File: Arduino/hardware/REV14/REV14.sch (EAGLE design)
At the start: 23 parts, among them IC2 ATMEGA168-AU, Q1 32768Hz, U2 RFM95WSMD

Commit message: updated rev 14
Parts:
- removed ANT: ANT (86 mm), wirepad:2,15/1,0
- removed C11: 100nF, resistor:C-EUC0603
- removed C8: 100u, SparkFun-Passives:CAP_POL1206
- removed R12, R5: 4.7K, resistor:R-EU_R0603
- removed U2: RFM95WSMD, misiek:RFM95WSMD
- added C5: 100nF, resistor:C-EUC0603
- added DQ: (no value), wirepad:2,15/1,0
- added R3: 4.7K, resistor:R-EU_R0603
- added U1: RN2483, RFM95W-RN2483:RN2483
- I2C_EXT: device pinhead:PINHD-2X7 -> pinhead:PINHD-2X10
- renumbered PHT1 to PHT, U$4 to U4
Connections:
- removed net N$22: ANT.P, U2.ANT
- new net RN2483_RESET: IC2.DIGITAL_5(PWM)
- new net RN2483_UART_RX: IC2.DIGITAL_4
- new net RN2483_UART_TX: IC2.DIGITAL_3(PWM)
- net D2: now also DQ.P, I2C_EXT.17; no longer I2C_EXT.14
- net GND: now also I2C_EXT.10, I2C_EXT.12; no longer C8.-, U2.GND@1, U2.GND@2, U2.GND@3
- net IO_POWER_UP: now also I2C_EXT.19
- net N$1: now also I2C_EXT.18, R3.2; no longer C11.2, I2C_EXT.5
- net N$3: now also I2C_EXT.16, R4.2; no longer I2C_EXT.12, R5.2
- net N$4: now also C5.2, I2C_EXT.20; no longer I2C_EXT.11, R4.2
- net RESET: now also C5.1, I2C_EXT.5; no longer C11.1
- net RFM_IRQ: now also I2C_EXT.13; no longer I2C_EXT.7
- net RX: now also R3.1; no longer R4.1
- net SDA: now also I2C_EXT.11; no longer I2C_EXT.10
- net SPI_MISO: no longer U2.MISO
- net SPI_MOSI: no longer U2.MOSI
- net SPI_NSS: now also I2C_EXT.15; no longer I2C_EXT.8, R12.1, U2.NSS
- net SPI_SCK: no longer U2.SCK
- net TX: now also R4.1; no longer R5.1
- net VCC: no longer C8.+, R12.2, U2.VCC
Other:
- note added: "On BOM"
- moved on the sheet: C4, R4

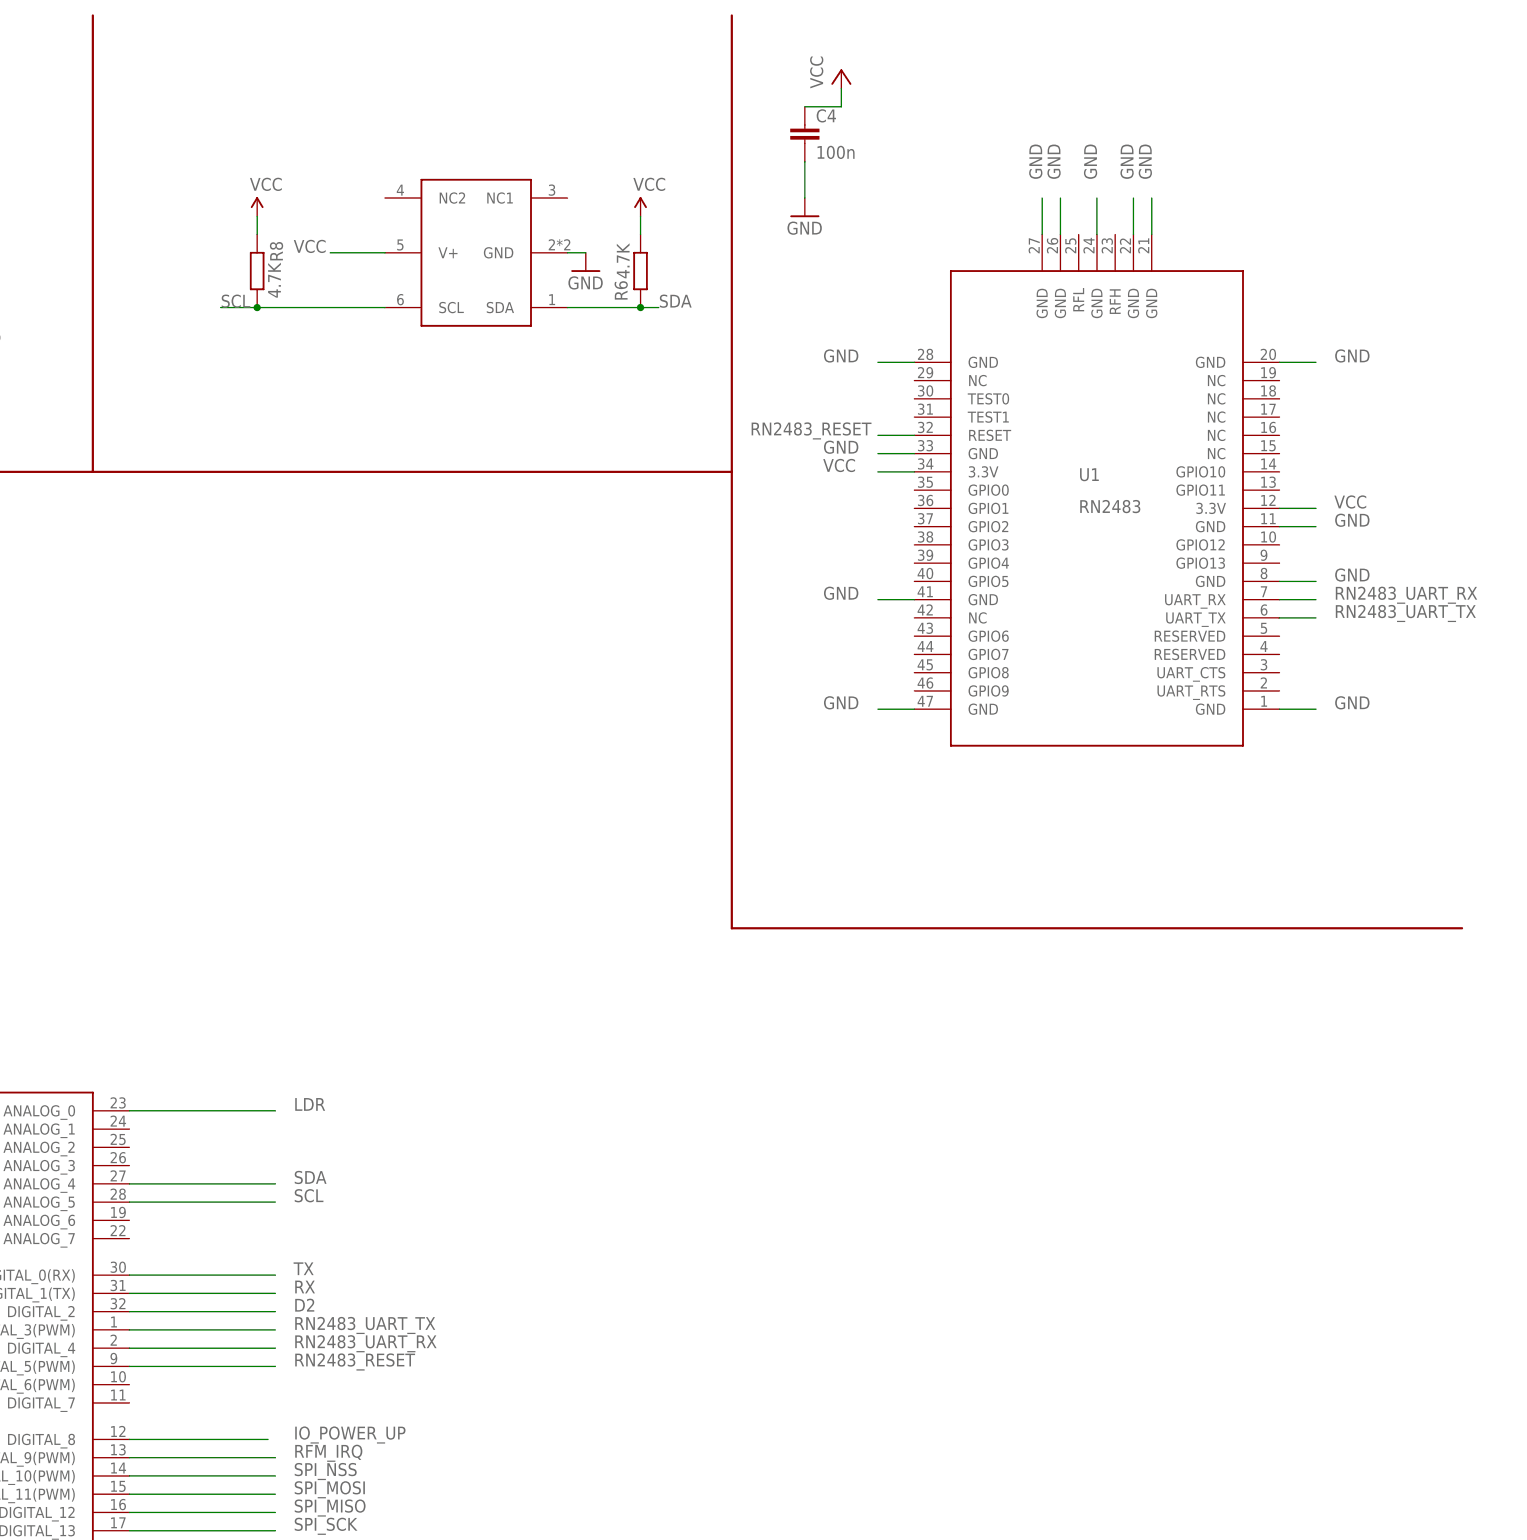
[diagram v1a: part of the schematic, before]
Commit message: rev 14 ant tracks and xtal done
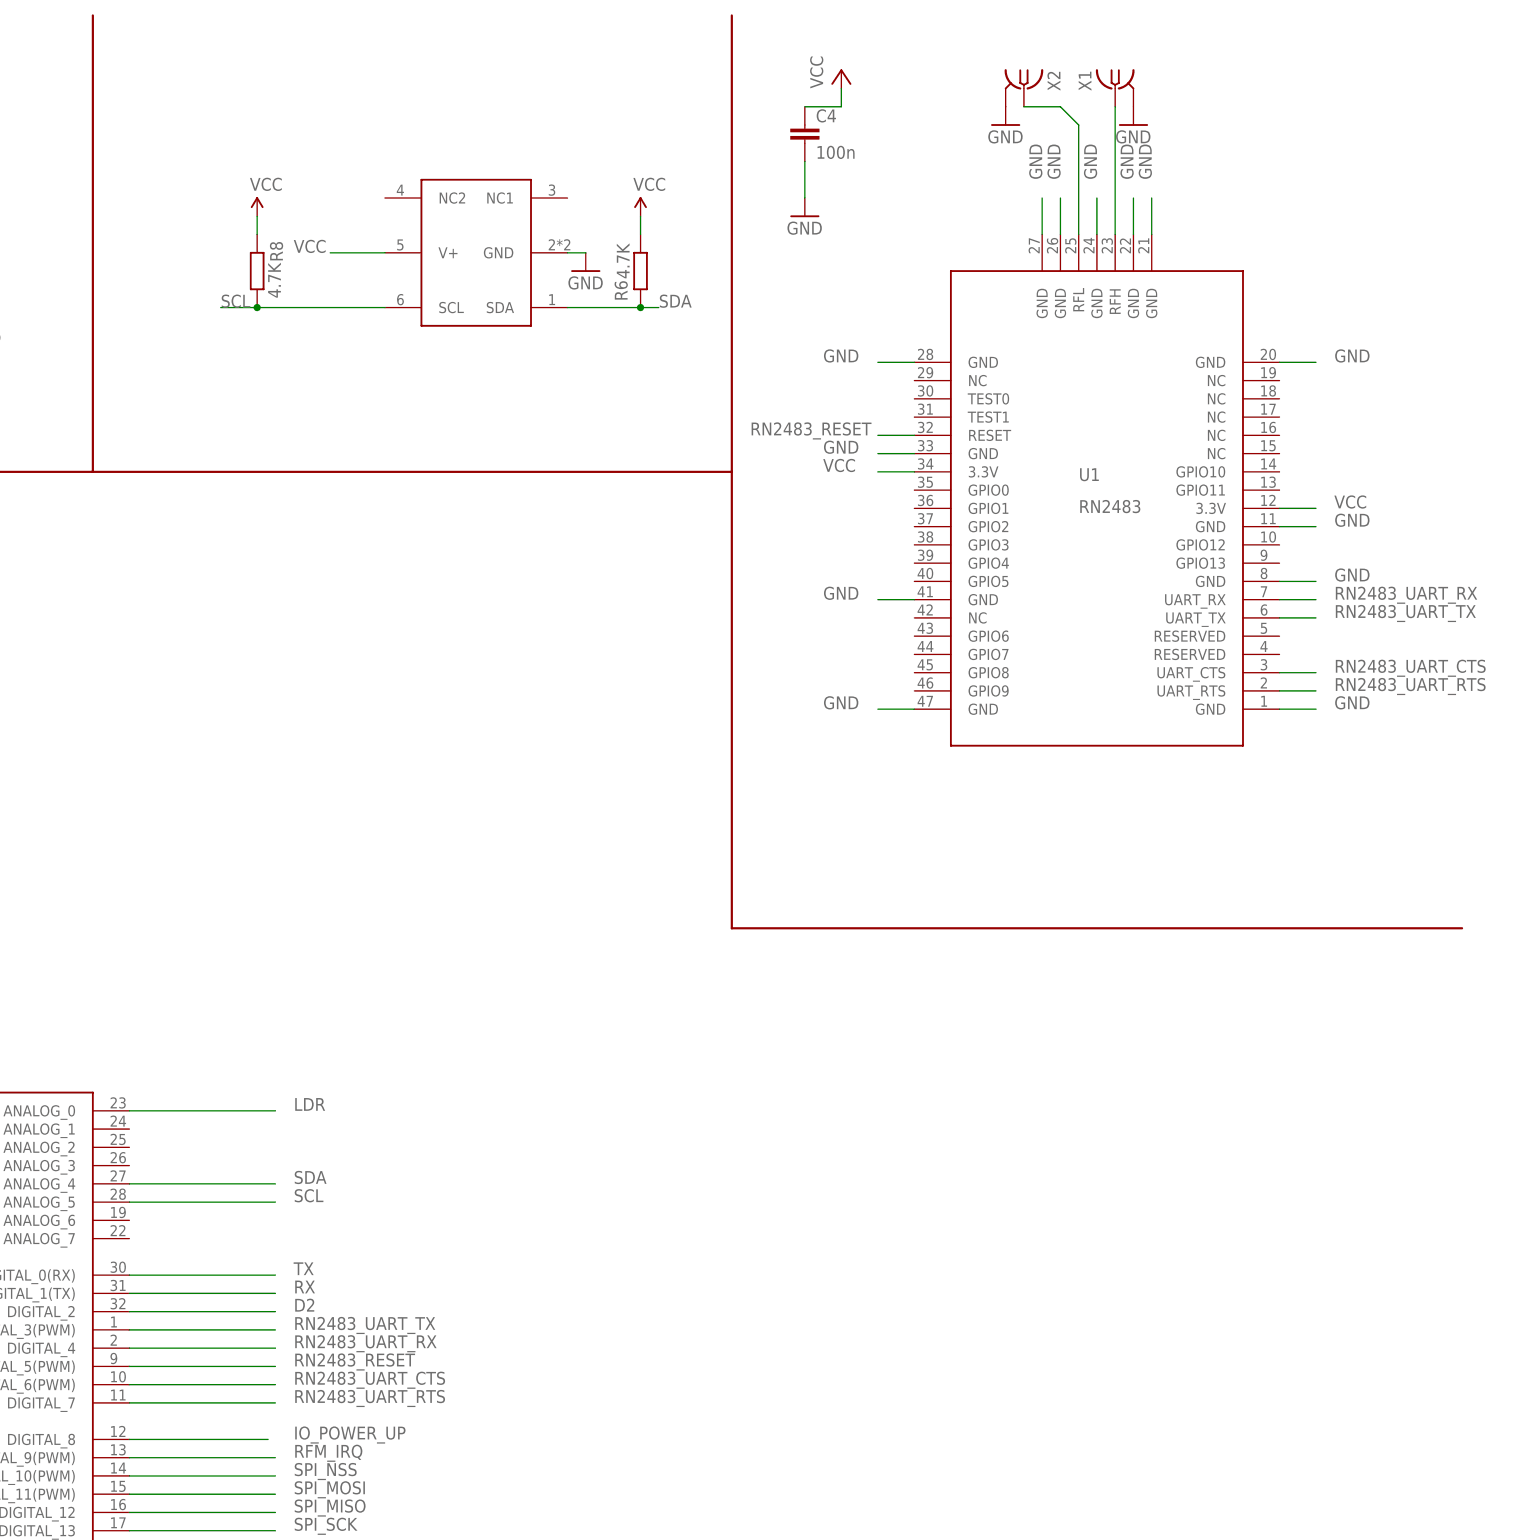
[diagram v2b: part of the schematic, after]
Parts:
- added X1, X2: SMA-142-0701-881/886, con-coax:SMA-142-0701-881/886
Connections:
- new net N$22: U1.RFH, X1.1
- new net N$33: U1.RFL, X2.1
- new net RN2483_UART_CTS: IC2.DIGITAL_6(PWM), U1.UART_CTS
- new net RN2483_UART_RTS: U1.UART_RTS
- net GND: now also U1.GND@1, U1.GND@10, U1.GND@11, U1.GND@12, U1.GND@13, U1.GND@2, U1.GND@3, U1.GND@4, U1.GND@5, U1.GND@6, U1.GND@7, U1.GND@8, U1.GND@9, X1.2, X2.2
- net RN2483_RESET: now also U1.RESET
- net RN2483_UART_RX: now also U1.UART_RX
- net RN2483_UART_TX: now also U1.UART_TX
- net VCC: now also U1.3.3V, U1.3.3V@1
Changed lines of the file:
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@@
 <part name="R4" library="resistor" deviceset="R-EU_" device="R0603" value="4.7K"/>
 <part name="C5" library="resistor" deviceset="C-EU" device="C0603" value="100nF"/>
+<part name="X1" library="con-coax" deviceset="SMA-" device="142-0701-881/886"/>
+<part name="X2" library="con-coax" deviceset="SMA-" device="142-0701-881/886"/>
+<part name="GND4" library="supply1" deviceset="GND" device=""/>
+<part name="GND5" library="supply1" deviceset="GND" device=""/>
 </parts>
 <sheets>
@@
 <attribute name="NAME" x="131.699" y="230.124" size="1.778" layer="95" rot="R90"/>
 </instance>
+<instance part="X1" gate="G1" x="335.28" y="246.38" smashed="yes" rot="MR270">
+<attribute name="NAME" x="331.978" y="248.92" size="1.778" layer="95" rot="MR270"/>
+</instance>
+<instance part="X2" gate="G1" x="322.58" y="246.38" smashed="yes" rot="R270">
+<attribute name="NAME" x="325.882" y="248.92" size="1.778" layer="95" rot="R270"/>
+</instance>
+<instance part="GND4" gate="1" x="320.04" y="241.3"/>
+<instance part="GND5" gate="1" x="337.82" y="241.3"/>
 </instances>
 <busses>
@@
 <wire x1="307.34" y1="208.28" x2="302.26" y2="208.28" width="0.1524" layer="91"/>
 <label x="294.64" y="208.28" size="1.778" layer="95"/>
+<pinref part="U1" gate="G$1" pin="GND@10"/>
 </segment>
 <segment>
 <wire x1="307.34" y1="195.58" x2="302.26" y2="195.58" width="0.1524" layer="91"/>
 <label x="294.64" y="195.58" size="1.778" layer="95"/>
+<pinref part="U1" gate="G$1" pin="GND@11"/>
 </segment>
 <segment>
 <wire x1="307.34" y1="175.26" x2="302.26" y2="175.26" width="0.1524" layer="91"/>
 <label x="294.64" y="175.26" size="1.778" layer="95"/>
+<pinref part="U1" gate="G$1" pin="GND@12"/>
 </segment>
 <segment>
 <wire x1="307.34" y1="160.02" x2="302.26" y2="160.02" width="0.1524" layer="91"/>
 <label x="294.64" y="160.02" size="1.778" layer="95"/>
+<pinref part="U1" gate="G$1" pin="GND@13"/>
 </segment>
 <segment>
 <wire x1="363.22" y1="208.28" x2="358.14" y2="208.28" width="0.1524" layer="91"/>
 <label x="365.76" y="208.28" size="1.778" layer="95"/>
+<pinref part="U1" gate="G$1" pin="GND@4"/>
 </segment>
 <segment>
 <wire x1="363.22" y1="185.42" x2="358.14" y2="185.42" width="0.1524" layer="91"/>
 <label x="365.76" y="185.42" size="1.778" layer="95"/>
+<pinref part="U1" gate="G$1" pin="GND@3"/>
 </segment>
 <segment>
 <wire x1="363.22" y1="177.8" x2="358.14" y2="177.8" width="0.1524" layer="91"/>
 <label x="365.76" y="177.8" size="1.778" layer="95"/>
+<pinref part="U1" gate="G$1" pin="GND@2"/>
 </segment>
 <segment>
 <wire x1="363.22" y1="160.02" x2="358.14" y2="160.02" width="0.1524" layer="91"/>
 <label x="365.76" y="160.02" size="1.778" layer="95"/>
+<pinref part="U1" gate="G$1" pin="GND@1"/>
 </segment>
 <segment>
 <wire x1="340.36" y1="226.06" x2="340.36" y2="231.14" width="0.1524" layer="91"/>
 <label x="340.36" y="233.68" size="1.778" layer="95" rot="R90"/>
+<pinref part="U1" gate="G$1" pin="GND@5"/>
 </segment>
 <segment>
 <wire x1="337.82" y1="226.06" x2="337.82" y2="231.14" width="0.1524" layer="91"/>
 <label x="337.82" y="233.68" size="1.778" layer="95" rot="R90"/>
+<pinref part="U1" gate="G$1" pin="GND@6"/>
 </segment>
 <segment>
 <wire x1="332.74" y1="226.06" x2="332.74" y2="231.14" width="0.1524" layer="91"/>
 <label x="332.74" y="233.68" size="1.778" layer="95" rot="R90"/>
+<pinref part="U1" gate="G$1" pin="GND@7"/>
 </segment>
 <segment>
 <wire x1="327.66" y1="226.06" x2="327.66" y2="231.14" width="0.1524" layer="91"/>
 <label x="327.66" y="233.68" size="1.778" layer="95" rot="R90"/>
+<pinref part="U1" gate="G$1" pin="GND@8"/>
 </segment>
 <segment>
 <wire x1="325.12" y1="226.06" x2="325.12" y2="231.14" width="0.1524" layer="91"/>
 <label x="325.12" y="233.68" size="1.778" layer="95" rot="R90"/>
+<pinref part="U1" gate="G$1" pin="GND@9"/>
 </segment>
 <segment>
@@
 <pinref part="I2C_EXT" gate="A" pin="12"/>
 <label x="114.3" y="223.52" size="1.778" layer="95"/>
+</segment>
+<segment>
+<pinref part="X2" gate="G1" pin="2"/>
+<pinref part="GND4" gate="1" pin="GND"/>
+</segment>
+<segment>
+<pinref part="X1" gate="G1" pin="2"/>
+<pinref part="GND5" gate="1" pin="GND"/>
 </segment>
 </net>
@@
 <wire x1="358.14" y1="187.96" x2="363.22" y2="187.96" width="0.1524" layer="91"/>
 <label x="365.76" y="187.96" size="1.778" layer="95"/>
+<pinref part="U1" gate="G$1" pin="3.3V"/>
 </segment>
 <segment>
 <wire x1="302.26" y1="193.04" x2="307.34" y2="193.04" width="0.1524" layer="91"/>
 <label x="294.64" y="193.04" size="1.778" layer="95"/>
+<pinref part="U1" gate="G$1" pin="3.3V@1"/>
 </segment>
 <segment>
@@
 <wire x1="358.14" y1="172.72" x2="363.22" y2="172.72" width="0.1524" layer="91"/>
 <label x="365.76" y="172.72" size="1.778" layer="95"/>
+<pinref part="U1" gate="G$1" pin="UART_TX"/>
 </segment>
 </net>
@@
 <wire x1="358.14" y1="175.26" x2="363.22" y2="175.26" width="0.1524" layer="91"/>
 <label x="365.76" y="175.26" size="1.778" layer="95"/>
+<pinref part="U1" gate="G$1" pin="UART_RX"/>
 </segment>
 </net>
@@
 <wire x1="302.26" y1="198.12" x2="307.34" y2="198.12" width="0.1524" layer="91"/>
 <label x="284.48" y="198.12" size="1.778" layer="95"/>
+<pinref part="U1" gate="G$1" pin="RESET"/>
 </segment>
 </net>
@@
 </segment>
 </net>
+<net name="RN2483_UART_CTS" class="0">
+<segment>
+<pinref part="IC2" gate="1" pin="DIGITAL_6(PWM)"/>
+<wire x1="198.12" y1="66.04" x2="218.44" y2="66.04" width="0.1524" layer="91"/>
+<label x="220.98" y="66.04" size="1.778" layer="95"/>
+</segment>
+<segment>
+<wire x1="358.14" y1="165.1" x2="363.22" y2="165.1" width="0.1524" layer="91"/>
+<label x="365.76" y="165.1" size="1.778" layer="95"/>
+<pinref part="U1" gate="G$1" pin="UART_CTS"/>
+</segment>
+</net>
+<net name="RN2483_UART_RTS" class="0">
+<segment>
+<pinref part="U1" gate="G$1" pin="UART_RTS"/>
+<wire x1="358.14" y1="162.56" x2="363.22" y2="162.56" width="0.1524" layer="91"/>
+<label x="365.76" y="162.56" size="1.778" layer="95"/>
+</segment>
+<segment>
+<wire x1="198.12" y1="63.5" x2="218.44" y2="63.5" width="0.1524" layer="91"/>
+<label x="220.98" y="63.5" size="1.778" layer="95"/>
+</segment>
+</net>
+<net name="N$22" class="2">
+<segment>
+<pinref part="U1" gate="G$1" pin="RFH"/>
+<pinref part="X1" gate="G1" pin="1"/>
+<wire x1="335.28" y1="226.06" x2="335.28" y2="243.84" width="0.1524" layer="91"/>
+</segment>
+</net>
+<net name="N$33" class="2">
+<segment>
+<pinref part="U1" gate="G$1" pin="RFL"/>
+<wire x1="330.2" y1="226.06" x2="330.2" y2="241.3" width="0.1524" layer="91"/>
+<pinref part="X2" gate="G1" pin="1"/>
+<wire x1="330.2" y1="241.3" x2="327.66" y2="243.84" width="0.1524" layer="91"/>
+<wire x1="327.66" y1="243.84" x2="322.58" y2="243.84" width="0.1524" layer="91"/>
+</segment>
+</net>

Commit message: rev14 ready for routing
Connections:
- net RN2483_UART_RTS: now also IC2.DIGITAL_7
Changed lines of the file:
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@@
 <wire x1="198.12" y1="63.5" x2="218.44" y2="63.5" width="0.1524" layer="91"/>
 <label x="220.98" y="63.5" size="1.778" layer="95"/>
+<pinref part="IC2" gate="1" pin="DIGITAL_7"/>
 </segment>
 </net>
